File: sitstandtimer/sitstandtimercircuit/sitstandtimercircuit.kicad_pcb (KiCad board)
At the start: 2 copper layers, 76.2 x 50.8 mm, 11 parts, among them SW1 SW_Push_SPDT, U1 Feather32u4, U2 .56-7segment-backpack, U3 DS3231, U4 .56-7segment-backpack, U5 Sonar-rcwl-1601

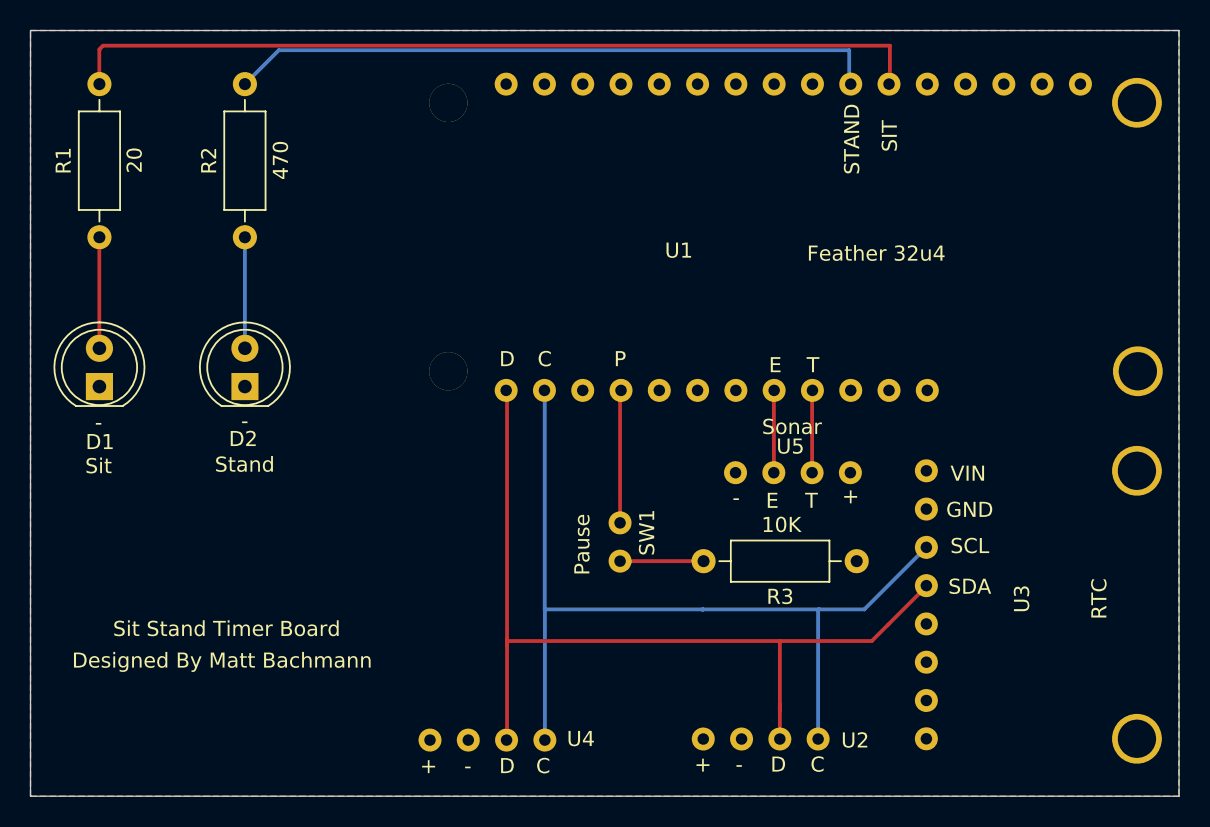
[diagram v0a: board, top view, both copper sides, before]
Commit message: board v2
More mounting holes

Larger holes for components mounted with breadboard headers
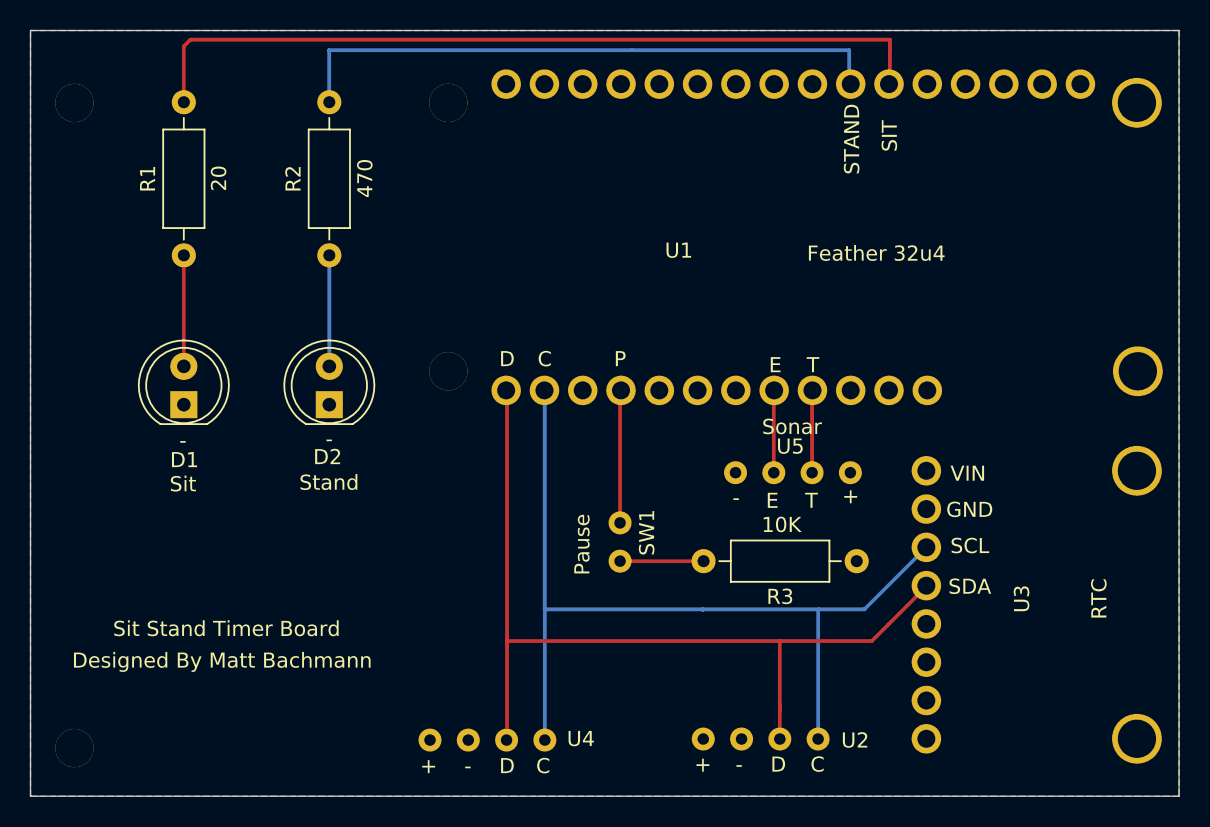
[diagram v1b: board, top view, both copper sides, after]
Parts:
- added REF**: drillhole, sitstandtimercircuit:drillhole, F.Cu at (183.0, 75.8)
- added REF**: drillhole, sitstandtimercircuit:drillhole, F.Cu at (183.0, 33.0)
- moved R1 5.73 mm to (190.3, 43.1)
- moved D1 5.73 mm to (190.3, 53.0)
- moved R2 5.73 mm to (199.9, 43.1)
- moved D2 5.73 mm to (199.9, 53.0)
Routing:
- net Net-(R1-Pad2): track 57.4 -> 53.8 mm
- net Net-(R2-Pad2): track 43.1 -> 39.9 mm
